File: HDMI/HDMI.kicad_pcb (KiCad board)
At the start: 2 copper layers, 39.5 x 25.1 mm, 33 parts, among them J2 PMOD, P1 HDMI-D, U1 NCP1402SN33T1G, U2 PCA9306

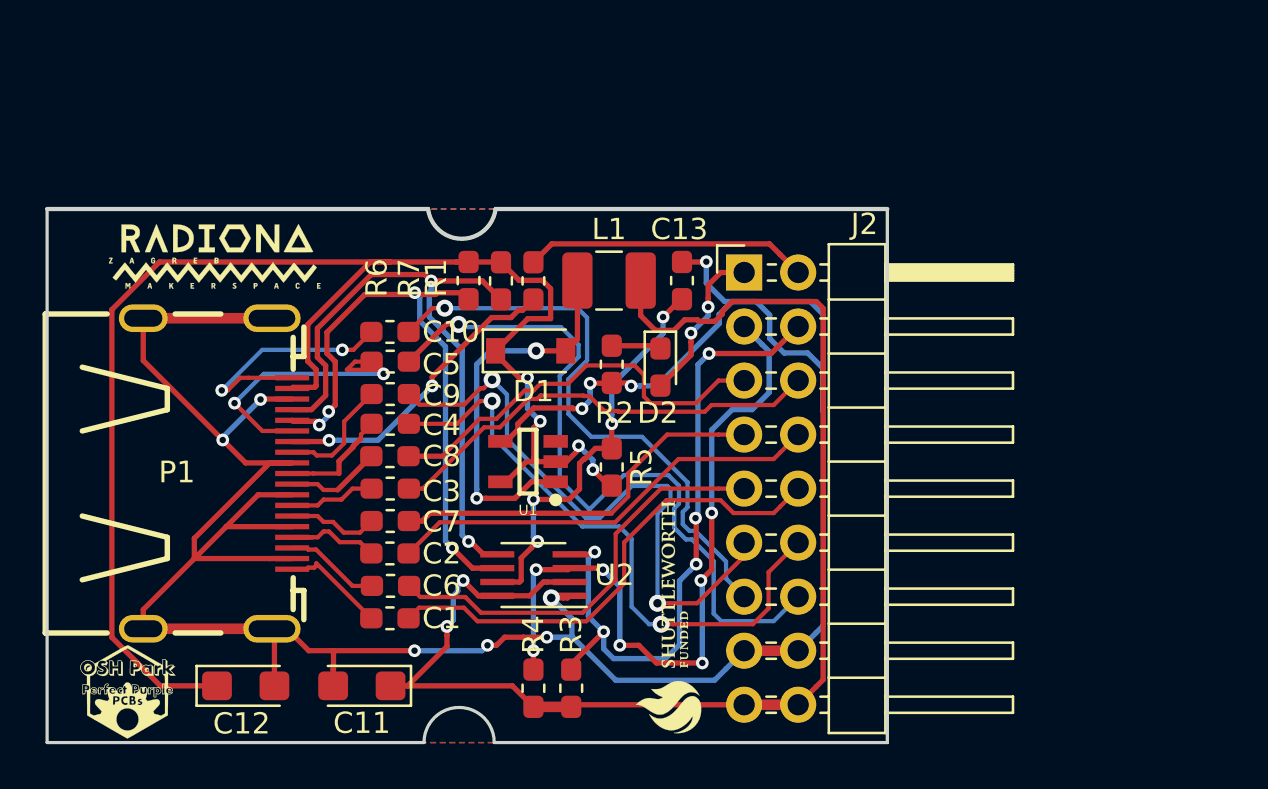
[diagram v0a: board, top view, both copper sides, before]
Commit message: Adding new HDMI version with new logos, and holes for screws
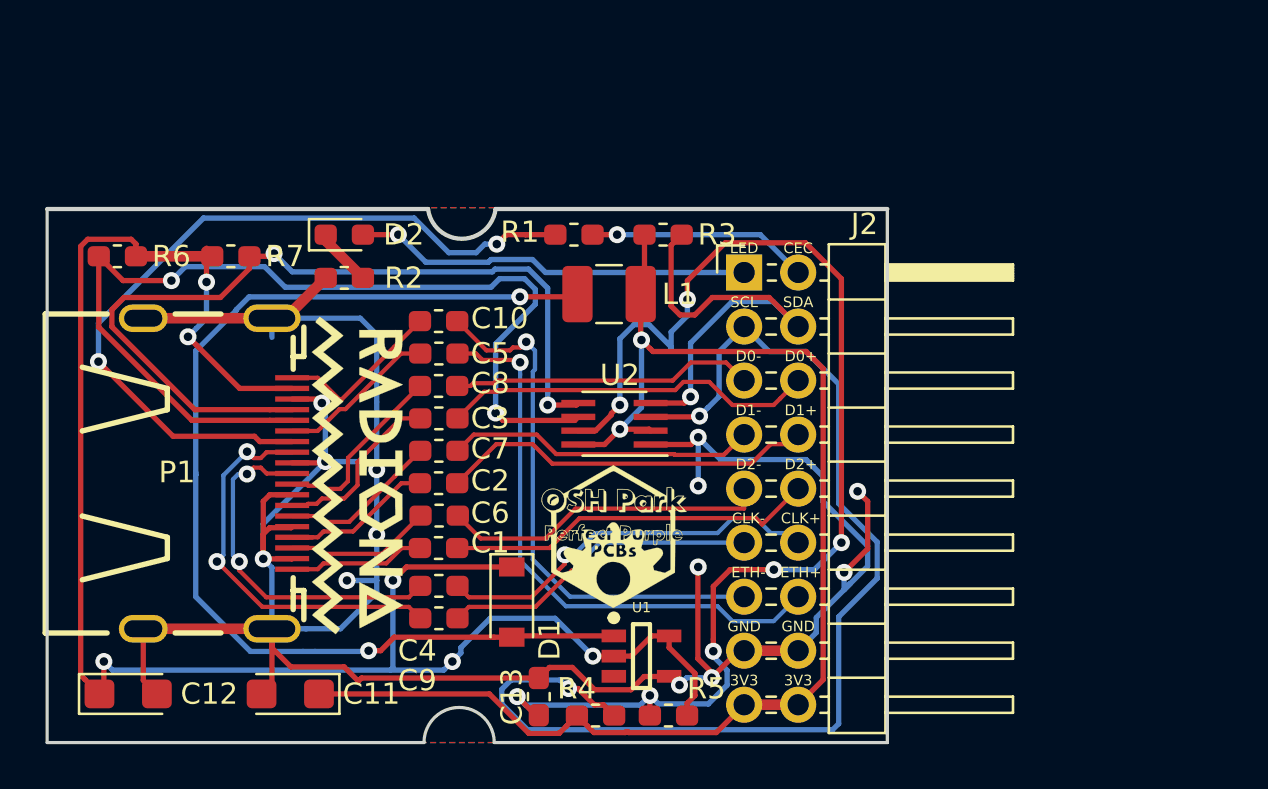
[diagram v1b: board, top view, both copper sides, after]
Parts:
- removed the G*** at (127.3, 77.0)
- removed the G*** at (114.8, 87.1)
- removed the G*** at (140.2, 83.6)
- removed the G*** at (118.9, 66.5)
- added G***: LOGO, parts2:OSH_7x7, F.Cu at (137.7, 79.9)
- added G***: LOGO, parts2:radiona, F.Cu at (125.6, 76.8)
- U1: value NCP1402SN33T1G -> NCP1402
- moved R3 21.8 mm to (140.0, 65.5), turned to 0 degrees
- moved C13 20.7 mm to (134.1, 87.2)
- moved R6 16.5 mm to (114.3, 66.5), turned to 180 degrees
- moved D2 16.1 mm to (125.0, 65.5), turned to 0 degrees
- moved G*** 15.5 mm to (118.9, 76.5), turned to 270 degrees
- moved R2 13.2 mm to (125.0, 67.6), turned to 180 degrees
- moved R7 12.8 mm to (119.6, 66.5), turned to 0 degrees
- moved R5 12.0 mm to (140.2, 88.1), turned to 180 degrees
- moved D1 11.8 mm to (132.8, 82.8), turned to 270 degrees
- moved C9 10.8 mm to (129.4, 83.6)
- moved U1 10.6 mm to (138.9, 85.3), turned to 0 degrees
- moved G*** 10.4 mm to (139.4, 77.0), turned to 270 degrees
- moved U2 8.07 mm to (137.7, 74.4)
- moved C4 7.96 mm to (129.4, 82.0)
- moved C12 5.54 mm to (114.8, 87.1)
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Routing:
- net Net-(C13-Pad1): track 19.2 -> 58.5 mm, vias 4 -> 7
- net Net-(D1-Pad2): track 18.3 -> 51.8 mm
- net /CEC: track 14.4 -> 37.3 mm
- net PMOD_SCL: track 34.3 -> 53.7 mm, vias 7 -> 2
- net GPDI_SCL: track 29.0 -> 47.0 mm, vias 4 -> 2
- net GPDI_CLK-: track 28.8 -> 15.2 mm, vias 2 -> 1
- net +5V: track 70.9 -> 84.3 mm, vias 4 -> 6
- net /CLK-: track 5.59 -> 18.8 mm, vias 0 -> 2
- net /CLK+: track 5.20 -> 16.8 mm, vias 0 -> 2
- net LED_HDMI: track 7.60 -> 18.8 mm, vias 2 -> 1
- net GPDI_SDA: track 30.0 -> 40.6 mm
- net PMOD_SDA: track 31.6 -> 21.5 mm, vias 5 -> 1
- net GPDI_CLK+: track 28.5 -> 18.5 mm, vias 2 -> 1
- net GPDI_ETH+: track 34.5 -> 27.2 mm
- net /ETH+: track 14.0 -> 7.53 mm, vias 2 -> 0
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
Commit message: Adding pullups for HDMI input
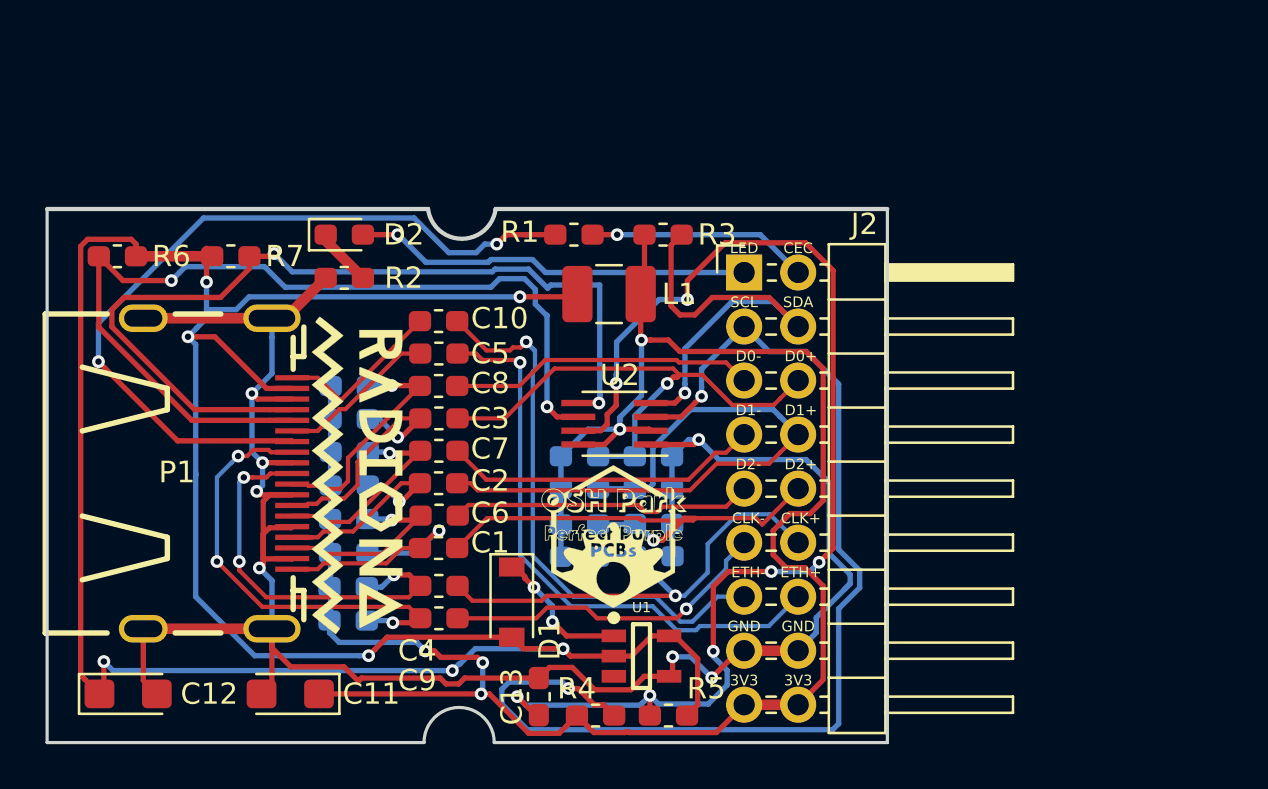
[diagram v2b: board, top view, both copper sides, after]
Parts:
- removed the G*** at (139.4, 77.0)
- added R10: 10K, Resistor_SMD:R_0603_1608Metric_Pad1.05x0.95mm_HandSolder, B.Cu at (139.5, 76.0)
- added R11: 50R, Resistor_SMD:R_0603_1608Metric_Pad1.05x0.95mm_HandSolder, B.Cu at (125.2, 78.9)
- added R12: 50R, Resistor_SMD:R_0603_1608Metric_Pad1.05x0.95mm_HandSolder, B.Cu at (125.2, 77.3)
- added R13: 10K, Resistor_SMD:R_0603_1608Metric_Pad1.05x0.95mm_HandSolder, B.Cu at (136.0, 77.5)
- added R14: 10K, Resistor_SMD:R_0603_1608Metric_Pad1.05x0.95mm_HandSolder, B.Cu at (139.5, 77.5)
- added R15: 50R, Resistor_SMD:R_0603_1608Metric_Pad1.05x0.95mm_HandSolder, B.Cu at (125.2, 75.8)
- added R16: 50R, Resistor_SMD:R_0603_1608Metric_Pad1.05x0.95mm_HandSolder, B.Cu at (125.2, 74.2)
- added R17: 10K, Resistor_SMD:R_0603_1608Metric_Pad1.05x0.95mm_HandSolder, B.Cu at (136.0, 79.2)
- added R18: 10K, Resistor_SMD:R_0603_1608Metric_Pad1.05x0.95mm_HandSolder, B.Cu at (139.5, 79.1)
- added R19: 50R, Resistor_SMD:R_0603_1608Metric_Pad1.05x0.95mm_HandSolder, B.Cu at (125.2, 72.7)
- added R20: 50R, Resistor_SMD:R_0603_1608Metric_Pad1.05x0.95mm_HandSolder, B.Cu at (125.2, 82.1)
- added R21: 10K, Resistor_SMD:R_0603_1608Metric_Pad1.05x0.95mm_HandSolder, B.Cu at (136.0, 80.7)
- added R22: 10K, Resistor_SMD:R_0603_1608Metric_Pad1.05x0.95mm_HandSolder, B.Cu at (139.5, 80.7)
- added R23: 50R, Resistor_SMD:R_0603_1608Metric_Pad1.05x0.95mm_HandSolder, B.Cu at (125.2, 83.7)
- added R8: 50R, Resistor_SMD:R_0603_1608Metric_Pad1.05x0.95mm_HandSolder, B.Cu at (125.2, 80.5)
- added R9: 10K, Resistor_SMD:R_0603_1608Metric_Pad1.05x0.95mm_HandSolder, B.Cu at (136.0, 76.0)
- U1: value NCP1402 -> NCP1402SN33T1G
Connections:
- D1 pad 1: +5V -> Net-(D1-Pad1)
- D1 pad 2: Net-(D1-Pad2) -> +5V
- L1 pad 2: Net-(D1-Pad2) -> +5V
- U1 pad 1: Net-(D1-Pad2) -> Net-(D1-Pad1)
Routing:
- net Net-(D1-Pad2): track 51.8 -> 0.00 mm, vias 2 -> 0
- net +5V: track 84.3 -> 122.2 mm, vias 6 -> 7
- net +3V3: track 63.5 -> 95.4 mm, vias 2 -> 5
- net GND: track 135.5 -> 103.8 mm, vias 13 -> 7
- net GPDI_D1+: track 17.7 -> 30.1 mm
- net GPDI_D0+: track 17.7 -> 24.7 mm, vias 0 -> 1
- net Net-(D1-Pad1): track 0.00 -> 6.05 mm, vias 0 -> 2
- net GPDI_D2+: track 17.4 -> 22.9 mm, vias 0 -> 1
- net GPDI_CLK+: track 18.5 -> 23.7 mm
- net /D2+: track 6.42 -> 11.3 mm, vias 0 -> 1
- net GPDI_SCL: track 47.0 -> 43.7 mm
- net /D0+: track 8.36 -> 11.5 mm, vias 0 -> 1
- net /D1+: track 8.03 -> 11.1 mm, vias 0 -> 1
- net /D2-: track 6.89 -> 9.50 mm, vias 0 -> 1
- net /CLK-: track 18.8 -> 21.4 mm, vias 2 -> 3
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- removed copper zone on B.Cu, net GND
- removed copper zone on F.Cu, net GND

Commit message: Changing DC-DC - rerouting
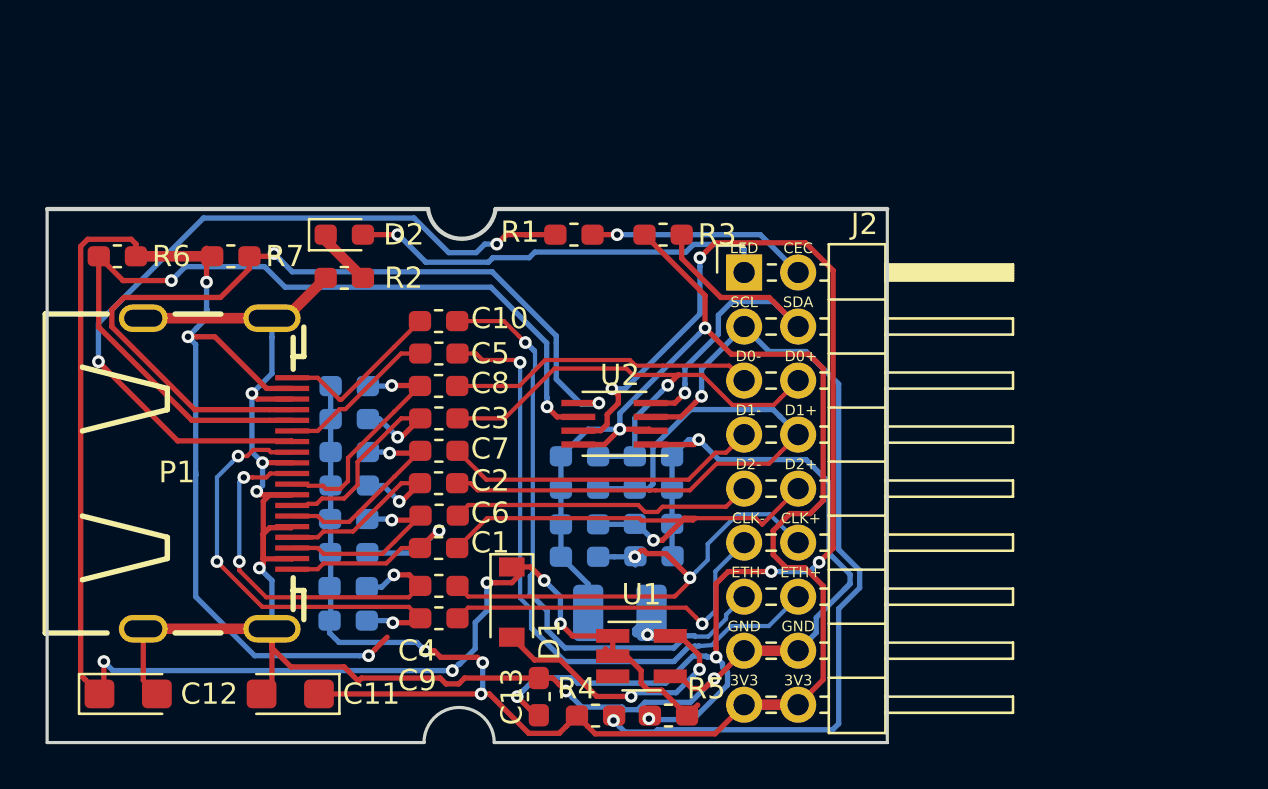
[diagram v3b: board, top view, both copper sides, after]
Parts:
- removed the G*** at (137.7, 79.9)
- removed the G*** at (125.6, 76.8)
- added G***: LOGO, parts2:radiona-small, B.Cu at (121.9, 87.1)
- added G***: LOGO, parts2:shutleworth, B.Cu at (128.8, 67.8)
- C12: value CP -> 47uF
- L1: value L -> 100u; moved to B.Cu
- U1: value NCP1402SN33T1G -> RN5RK501A; footprint NCP1402SN33T1G:SOT95P275X110-5N -> Package_TO_SOT_SMD:SOT-23-5_HandSoldering
- moved L1 15.0 mm to (137.9, 83.3), turned to 0 degrees
- moved G*** 0.25 mm to (118.6, 76.5)
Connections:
- D1 pad 1: Net-(D1-Pad1) -> +5V
- D1 pad 2: +5V -> Net-(D1-Pad2)
- L1 pad 2: +5V -> Net-(D1-Pad2)
- U1 pad 1: Net-(D1-Pad1) -> +5V
- U1 pad 5: +5V -> Net-(D1-Pad2)
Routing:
- net +5V: track 122.2 -> 100.7 mm, vias 7 -> 8
- net Net-(D1-Pad2): track 0.00 -> 15.7 mm, vias 0 -> 3
- net PMOD_SCL: track 52.5 -> 40.2 mm
- net Net-(D1-Pad1): track 6.05 -> 0.00 mm, vias 2 -> 0
- net Net-(C13-Pad1): track 56.1 -> 59.4 mm
- net +3V3: track 95.4 -> 98.4 mm
- net GPDI_ETH+: track 27.4 -> 30.3 mm
- net PMOD_SDA: track 21.2 -> 18.5 mm
- net GPDI_SDA: track 42.7 -> 40.4 mm
- net GPDI_ETH-: track 27.1 -> 29.3 mm
- net GPDI_SCL: track 43.7 -> 42.2 mm
- net LED_HDMI: track 18.8 -> 20.0 mm
- net GND: track 103.8 -> 104.9 mm
- net GPDI_CLK-: track 15.6 -> 16.7 mm
- net GPDI_CLK+: track 23.7 -> 24.4 mm, vias 1 -> 2

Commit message: Rerouting all, placing most components on top layer
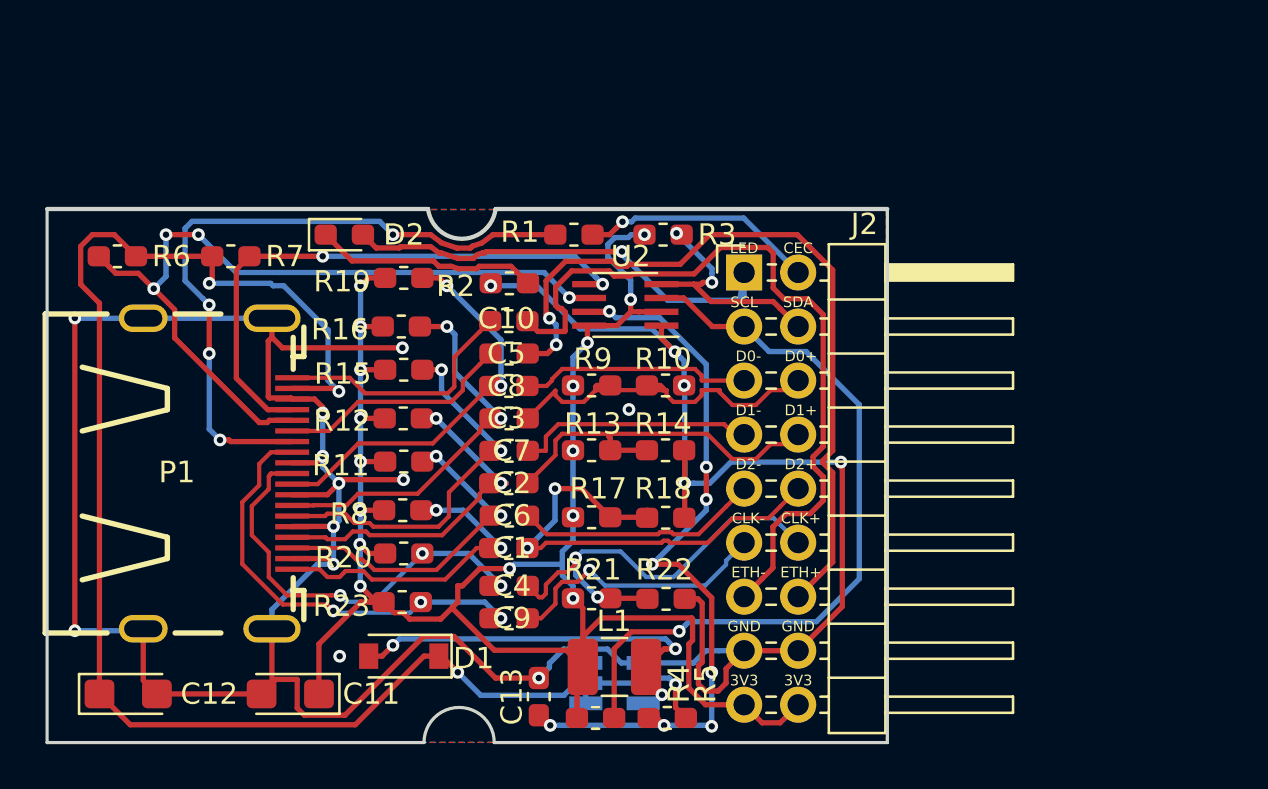
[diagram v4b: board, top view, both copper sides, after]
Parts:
- L1, R10, R11, R12, R13, R14, R15, R16, R17, R18, R19, R20, R21, R22, R23, R8, R9: moved to F.Cu
- U1: moved to B.Cu
- moved R2 7.77 mm to (132.7, 67.8)
- moved R19 5.69 mm to (127.8, 67.6)
- moved D1 5.68 mm to (127.8, 85.3), turned to 180 degrees
- moved U2 5.61 mm to (138.2, 68.8)
- moved R16 4.99 mm to (127.6, 69.8)
- moved R15 4.64 mm to (127.8, 71.9)
- moved R12 4.05 mm to (127.7, 74.2)
- moved R11 3.74 mm to (127.8, 76.2)
- moved R10 3.38 mm to (140.1, 72.6)
- moved R9 3.38 mm to (136.6, 72.6)
- moved C6 3.30 mm to (132.7, 78.7)
- moved C1 3.30 mm to (132.7, 80.3)
- moved C10 3.30 mm to (132.7, 69.6)
- moved C2 3.30 mm to (132.7, 77.2)
- moved C3 3.30 mm to (132.7, 74.2)
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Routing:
- net GND: track 104.9 -> 152.5 mm, vias 7 -> 17
- net +5V: track 100.7 -> 74.5 mm, vias 8 -> 4
- net Net-(C13-Pad1): track 59.4 -> 36.1 mm, vias 7 -> 8
- net GPDI_SDA: track 40.4 -> 27.0 mm
- net GPDI_D1+: track 30.1 -> 17.6 mm
- net /D1-: track 10.0 -> 18.1 mm, vias 1 -> 2
- net Net-(D2-Pad1): track 2.76 -> 10.5 mm
- net /D0-: track 11.2 -> 18.8 mm, vias 1 -> 2
- net GPDI_D0+: track 24.6 -> 17.2 mm, vias 1 -> 0
- net PMOD_SDA: track 18.5 -> 11.1 mm, vias 1 -> 2
- net /D2-: track 9.50 -> 16.3 mm, vias 1 -> 2
- net GPDI_ETH-: track 29.3 -> 36.0 mm, vias 1 -> 0
- net /D0+: track 11.5 -> 18.2 mm, vias 1 -> 2
- net GPDI_ETH+: track 30.3 -> 36.4 mm, vias 1 -> 2
- net +3V3: track 98.4 -> 92.7 mm, vias 5 -> 16
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- added copper zone on B.Cu, net GND
- added copper zone on F.Cu, net GND

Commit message: Finished PCB routing, adding new zipped gerbers
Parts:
- removed the G*** at (121.9, 87.1)
- removed the G*** at (128.8, 67.8)
- added G***: LOGO, parts2:radiona-10mm, B.Cu at (118.6, 66.8)
- added G***: LOGO, parts2:radiona-10mm, B.Cu at (118.4, 86.6)
- added G***: LOGO, parts2:shutleworth-12mm, B.Cu at (118.1, 76.5)
- added JP1: JUMP, Jumper:SolderJumper-2_P1.3mm_Bridged_RoundedPad1.0x1.5mm, B.Cu at (126.5, 87.4)
- added JP2: JUMP, Jumper:SolderJumper-2_P1.3mm_Bridged_RoundedPad1.0x1.5mm, B.Cu at (138.2, 71.4)
- added JP3: JUMP, Jumper:SolderJumper-2_P1.3mm_Bridged_RoundedPad1.0x1.5mm, B.Cu at (138.3, 74.2)
- added JP4: JUMP, Jumper:SolderJumper-2_P1.3mm_Bridged_RoundedPad1.0x1.5mm, B.Cu at (138.3, 77.2)
- added JP5: JUMP, Jumper:SolderJumper-2_P1.3mm_Bridged_RoundedPad1.0x1.5mm, B.Cu at (138.9, 83.3)
- added JP6: JUMP, Jumper:SolderJumper-2_P1.3mm_Bridged_RoundedPad1.0x1.5mm, B.Cu at (132.3, 85.9)
- added R24: 200R, Resistor_SMD:R_0603_1608Metric_Pad1.05x0.95mm_HandSolder, B.Cu at (149.4, 79.0)
- added R25: 200R, Resistor_SMD:R_0603_1608Metric_Pad1.05x0.95mm_HandSolder, B.Cu at (149.4, 72.9)
- added R26: 200R, Resistor_SMD:R_0603_1608Metric_Pad1.05x0.95mm_HandSolder, B.Cu at (149.4, 68.8)
- added R27: 200R, Resistor_SMD:R_0603_1608Metric_Pad1.05x0.95mm_HandSolder, B.Cu at (149.4, 83.2)
- C11: value CP -> 47uF
- moved G*** 9.67 mm to (128.3, 77.0), turned to 180 degrees
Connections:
- C12 pad 1: +5V -> Net-(C12-Pad1)
- D1 pad 1: +5V -> Net-(C12-Pad1)
- R10 pad 1: GPDI_D0+ -> Net-(JP2-Pad1)
- R11 pad 1: +3V3 -> Net-(JP1-Pad2)
- R12 pad 1: +3V3 -> Net-(JP1-Pad2)
- R13 pad 2: GPDI_D1+ -> Net-(JP3-Pad1)
- R14 pad 1: GPDI_D1+ -> Net-(JP3-Pad1)
- R15 pad 1: +3V3 -> Net-(JP1-Pad2)
- R16 pad 1: +3V3 -> Net-(JP1-Pad2)
- R17 pad 2: GPDI_D2+ -> Net-(JP4-Pad1)
- R18 pad 1: GPDI_D2+ -> Net-(JP4-Pad1)
- R19 pad 1: +3V3 -> Net-(JP1-Pad2)
- R20 pad 1: +3V3 -> Net-(JP1-Pad2)
- R21 pad 2: GPDI_CLK+ -> Net-(JP5-Pad1)
- R22 pad 1: GPDI_CLK+ -> Net-(JP5-Pad1)
- R23 pad 1: +3V3 -> Net-(JP1-Pad2)
- R8 pad 1: +3V3 -> Net-(JP1-Pad2)
- R9 pad 2: GPDI_D0+ -> Net-(JP2-Pad1)
- U1 pad 1: +5V -> Net-(C12-Pad1)
- U1 pad 2: +5V -> Net-(C12-Pad1)
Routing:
- net Net-(JP1-Pad2): track 0.00 -> 37.6 mm, vias 0 -> 7
- net Net-(C12-Pad1): track 0.00 -> 32.7 mm, vias 0 -> 2
- net +3V3: track 92.7 -> 68.6 mm, vias 16 -> 9
- net GPDI_D0-: track 10.9 -> 20.0 mm, vias 0 -> 1
- net GND: track 152.5 -> 161.5 mm, vias 17 -> 18
- net GPDI_D2-: track 11.5 -> 19.3 mm, vias 0 -> 2
- net GPDI_CLK+: track 21.0 -> 28.8 mm, vias 2 -> 4
- net GPDI_CLK-: track 12.8 -> 20.2 mm, vias 1 -> 3
- net GPDI_D1-: track 11.3 -> 18.6 mm, vias 0 -> 2
- net GPDI_ETH+: track 36.4 -> 42.6 mm
- net GPDI_D0+: track 17.2 -> 21.6 mm, vias 0 -> 4
- net Net-(JP4-Pad1): track 0.00 -> 3.46 mm, vias 0 -> 1
- net GPDI_D1+: track 17.6 -> 21.0 mm, vias 0 -> 2
- net Net-(JP3-Pad1): track 0.00 -> 3.04 mm, vias 0 -> 1
- net Net-(JP2-Pad1): track 0.00 -> 2.82 mm, vias 0 -> 1
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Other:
- board text added: "V_1.2"
